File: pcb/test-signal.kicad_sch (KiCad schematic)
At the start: 36 parts, among them J5 731000105, U84 FSA553, U85 LM27761, U87 AD5683RARMZ, U94 MAX4489AUA+

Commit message: Update PCB component part numbers
Replace and fill missing MPN and OEPSPN properties.
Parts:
- C128: MPN (none) -> CC0402JRNPO9BN101; OEPSPN (none) -> OEPS010089
- C129, C131, C96: MPN (none) -> C0402C182J5RACTU; OEPSPN (none) -> OEPS010090
- C130, C132: MPN (none) -> DNP; OEPSPN (none) -> OEPS000000
- R267, R291: MPN RG1005P-104-B-T5 -> AC0402FR-07100KL; OEPSPN OEPS020175 -> OEPS020051
- R268: MPN RG1005P-104-B-T5 -> RMCF0402FT249K; OEPSPN OEPS020175 -> OEPS020209
- R269, R293, R294, R298, R299, R300: MPN (none) -> ERA-1AEB102C; OEPSPN (none) -> OEPS020189
- R292: MPN (none) -> RT0805BRE079KL; OEPSPN (none) -> OEPS020207
- R295, R296: MPN (none) -> RMCF0402FT10R0; OEPSPN (none) -> OEPS020205
- R297: MPN (none) -> PNM0402E5001BST1; OEPSPN (none) -> OEPS020206
- U84: MPN (none) -> FSA553UCX; OEPSPN (none) -> OEPS080198
- U85: MPN (none) -> LM27761DSGR; OEPSPN (none) -> OEPS080196
- U94: MPN (none) -> MAX4489AUA+; OEPSPN (none) -> OEPS080197
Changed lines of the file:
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@@
 			)
 		)
-		(property "MPN" ""
+		(property "MPN" "C0402C182J5RACTU"
 			(at 133.35 115.57 0)
 			(effects
@@
 			)
 		)
-		(property "OEPSPN" ""
+		(property "OEPSPN" "OEPS010090"
 			(at 133.35 115.57 0)
 			(effects
@@
 			)
 		)
+		(property "MPN" "MAX4489AUA+"
+			(at 161.29 36.83 0)
+			(effects
+				(font
+					(size 1.27 1.27)
+				)
+				(hide yes)
+			)
+		)
+		(property "OEPSPN" "OEPS080197"
+			(at 161.29 36.83 0)
+			(effects
+				(font
+					(size 1.27 1.27)
+				)
+				(hide yes)
+			)
+		)
 		(pin "3"
 		)
@@
 			)
 		)
-		(property "MPN" ""
+		(property "MPN" "DNP"
 			(at 157.48 73.66 0)
 			(effects
@@
 			)
 		)
-		(property "OEPSPN" ""
+		(property "OEPSPN" "OEPS000000"
 			(at 157.48 73.66 0)
 			(effects
@@
 			)
 		)
-		(property "MPN" ""
+		(property "MPN" "ERA-1AEB102C"
 			(at 195.58 104.14 0)
 			(effects
@@
 			)
 		)
-		(property "OEPSPN" ""
+		(property "OEPSPN" "OEPS020189"
 			(at 195.58 104.14 0)
 			(effects
@@
 			)
 		)
-		(property "MPN" ""
+		(property "MPN" "C0402C182J5RACTU"
 			(at 157.48 62.23 0)
 			(effects
@@
 			)
 		)
-		(property "OEPSPN" ""
+		(property "OEPSPN" "OEPS010090"
 			(at 157.48 62.23 0)
 			(effects
@@
 			)
 		)
+		(property "MPN" "FSA553UCX"
+			(at 80.01 34.29 0)
+			(effects
+				(font
+					(size 1.27 1.27)
+				)
+				(hide yes)
+			)
+		)
+		(property "OEPSPN" "OEPS080198"
+			(at 80.01 34.29 0)
+			(effects
+				(font
+					(size 1.27 1.27)
+				)
+				(hide yes)
+			)
+		)
 		(pin "C1"
 		)
@@
 			)
 		)
+		(property "MPN" "MAX4489AUA+"
+			(at 163.83 36.83 0)
+			(effects
+				(font
+					(size 1.27 1.27)
+				)
+				(hide yes)
+			)
+		)
+		(property "OEPSPN" "OEPS080197"
+			(at 163.83 36.83 0)
+			(effects
+				(font
+					(size 1.27 1.27)
+				)
+				(hide yes)
+			)
+		)
 		(pin "3"
 		)
@@
 			)
 		)
-		(property "MPN" ""
+		(property "MPN" "ERA-1AEB102C"
 			(at 157.48 82.55 0)
 			(effects
@@
 			)
 		)
-		(property "OEPSPN" ""
+		(property "OEPSPN" "OEPS020189"
 			(at 157.48 82.55 0)
 			(effects
@@
 			)
 		)
-		(property "MPN" "RG1005P-104-B-T5"
+		(property "MPN" "AC0402FR-07100KL"
 			(at 115.57 162.56 0)
 			(effects
@@
 			)
 		)
-		(property "OEPSPN" "OEPS020175"
+		(property "OEPSPN" "OEPS020051"
 			(at 115.57 162.56 0)
 			(effects
@@
 			)
 		)
-		(property "MPN" ""
+		(property "MPN" "RMCF0402FT10R0"
 			(at 127 36.83 0)
 			(effects
@@
 			)
 		)
-		(property "OEPSPN" ""
+		(property "OEPSPN" "OEPS020205"
 			(at 127 36.83 0)
 			(effects
@@
 			)
 		)
-		(property "MPN" "RG1005P-104-B-T5"
+		(property "MPN" "RMCF0402FT249K"
 			(at 97.79 175.26 0)
 			(effects
@@
 			)
 		)
-		(property "OEPSPN" "OEPS020175"
+		(property "OEPSPN" "OEPS020209"
 			(at 97.79 175.26 0)
 			(effects
@@
 			)
 		)
+		(property "MPN" "LM27761DSGR"
+			(at 69.85 165.1 0)
+			(effects
+				(font
+					(size 1.27 1.27)
+				)
+				(hide yes)
+			)
+		)
+		(property "OEPSPN" "OEPS080196"
+			(at 69.85 165.1 0)
+			(effects
+				(font
+					(size 1.27 1.27)
+				)
+				(hide yes)
+			)
+		)
 		(pin "1"
 		)
@@
 			)
 		)
-		(property "MPN" ""
+		(property "MPN" "ERA-1AEB102C"
 			(at 175.26 114.3 0)
 			(effects
@@
 			)
 		)
-		(property "OEPSPN" ""
+		(property "OEPSPN" "OEPS020189"
 			(at 175.26 114.3 0)
 			(effects
@@
 			)
 		)
-		(property "MPN" ""
+		(property "MPN" "RMCF0402FT10R0"
 			(at 113.03 106.68 0)
 			(effects
@@
 			)
 		)
-		(property "OEPSPN" ""
+		(property "OEPSPN" "OEPS020205"
 			(at 113.03 106.68 0)
 			(effects
@@
 			)
 		)
-		(property "MPN" ""
+		(property "MPN" "PNM0402E5001BST1"
 			(at 163.83 137.16 0)
 			(effects
@@
 			)
 		)
-		(property "OEPSPN" ""
+		(property "OEPSPN" "OEPS020206"
 			(at 163.83 137.16 0)
 			(effects
@@
 			)
 		)
-		(property "MPN" ""
+		(property "MPN" "ERA-1AEB102C"
 			(at 133.35 137.16 0)
 			(effects
@@
 			)
 		)
-		(property "OEPSPN" ""
+		(property "OEPSPN" "OEPS020189"
 			(at 133.35 137.16 0)
 			(effects
@@
 			)
 		)
-		(property "MPN" ""
+		(property "MPN" "CC0402JRNPO9BN101"
 			(at 191.77 45.72 0)
 			(effects
@@
 			)
 		)
-		(property "OEPSPN" ""
+		(property "OEPSPN" "OEPS010089"
 			(at 191.77 45.72 0)
 			(effects
@@
 			)
 		)
+		(property "MPN" "FSA553UCX"
+			(at 80.01 104.14 0)
+			(effects
+				(font
+					(size 1.27 1.27)
+				)
+				(hide yes)
+			)
+		)
+		(property "OEPSPN" "OEPS080198"
+			(at 80.01 104.14 0)
+			(effects
+				(font
+					(size 1.27 1.27)
+				)
+				(hide yes)
+			)
+		)
 		(pin "C1"
 		)
@@
 			)
 		)
-		(property "MPN" ""
+		(property "MPN" "C0402C182J5RACTU"
 			(at 162.56 115.57 0)
 			(effects
@@
 			)
 		)
-		(property "OEPSPN" ""
+		(property "OEPSPN" "OEPS010090"
 			(at 162.56 115.57 0)
 			(effects
@@
 			)
 		)
-		(property "MPN" ""
+		(property "MPN" "DNP"
 			(at 133.35 127 0)
 			(effects
@@
 			)
 		)
-		(property "OEPSPN" ""
+		(property "OEPSPN" "OEPS000000"
 			(at 133.35 127 0)
 			(effects
@@
 			)
 		)
-		(property "MPN" ""
+		(property "MPN" "ERA-1AEB102C"
 			(at 204.47 44.45 0)
 			(effects
@@
 			)
 		)
-		(property "OEPSPN" ""
+		(property "OEPSPN" "OEPS020189"
 			(at 204.47 44.45 0)
 			(effects
@@
 			)
 		)
-		(property "MPN" ""
+		(property "MPN" "RT0805BRE079KL"
 			(at 217.17 34.29 0)
 			(effects
@@
 			)
 		)
-		(property "OEPSPN" ""
+		(property "OEPSPN" "OEPS020207"
 			(at 217.17 34.29 0)
 			(effects
@@
 			)
 		)
-		(property "MPN" ""
+		(property "MPN" "ERA-1AEB102C"
 			(at 184.15 104.14 0)
 			(effects
@@
 			)
 		)
-		(property "OEPSPN" ""
+		(property "OEPSPN" "OEPS020189"
 			(at 184.15 104.14 0)
 			(effects
@@
 			)
 		)
-		(property "MPN" "RG1005P-104-B-T5"
+		(property "MPN" "AC0402FR-07100KL"
 			(at 105.41 162.56 0)
 			(effects
@@
 			)
 		)
-		(property "OEPSPN" "OEPS020175"
+		(property "OEPSPN" "OEPS020051"
 			(at 105.41 162.56 0)
 			(effects
@@
 			(at 135.89 106.68 0)
 			(effects
+				(font
+					(size 1.27 1.27)
+				)
+				(hide yes)
+			)
+		)
+		(property "MPN" "MAX4489AUA+"
+			(at 135.89 106.68 0)
+			(effects
+				(font
+					(size 1.27 1.27)
+				)
+				(hide yes)
+			)
+		)
+		(property "OEPSPN" "OEPS080197"
+			(at 135.89 106.68 0)
+			(effects

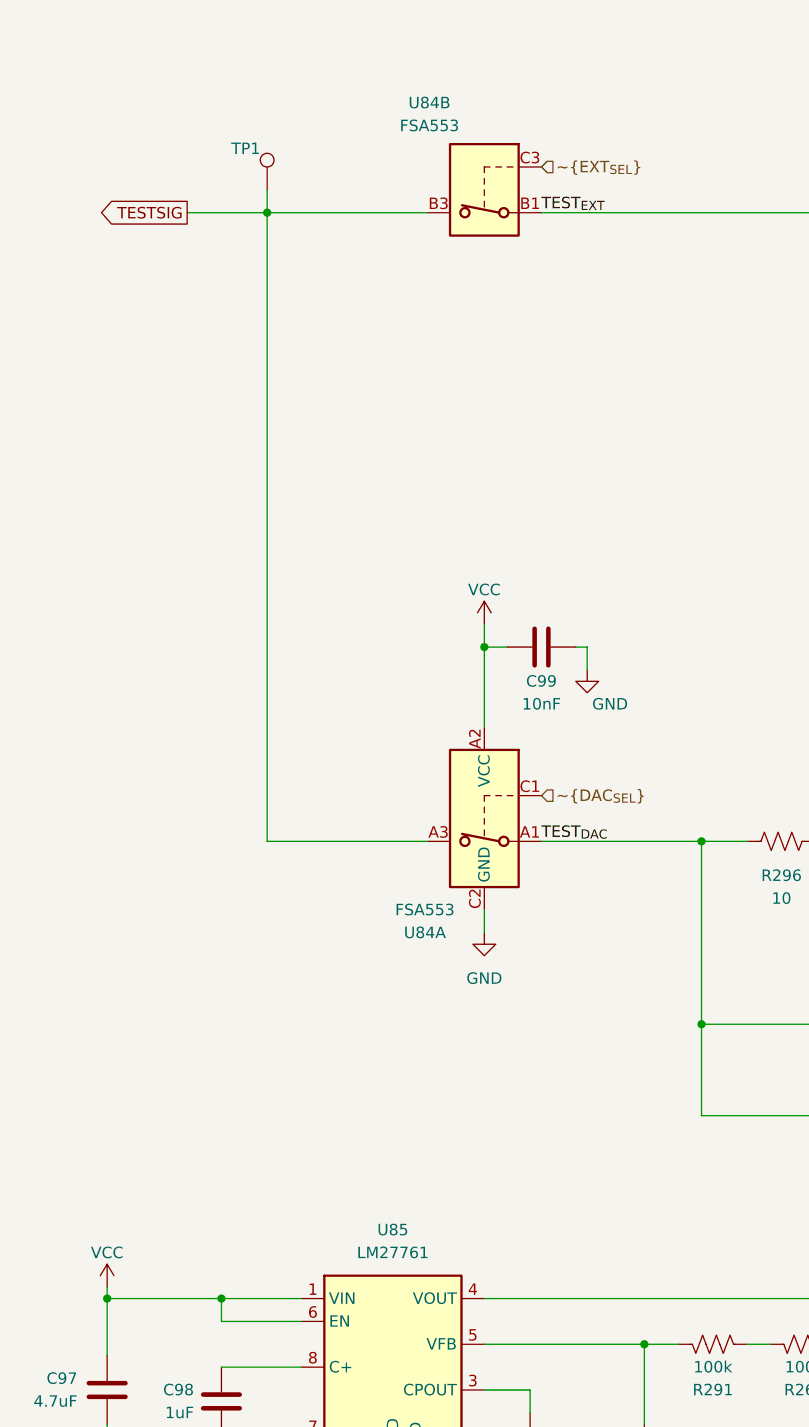
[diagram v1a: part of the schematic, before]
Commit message: Updated OEPS PN and regenerated BOM and PnP files
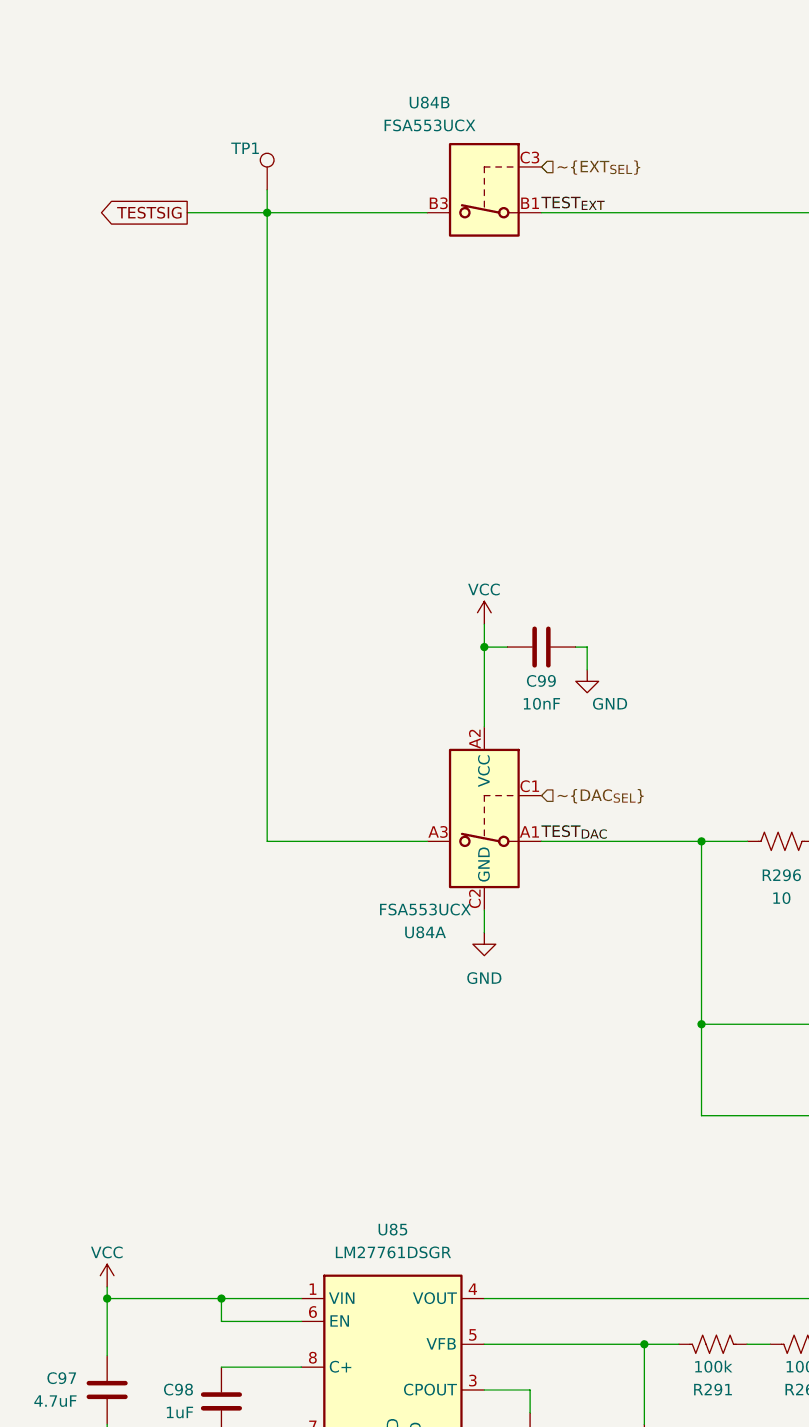
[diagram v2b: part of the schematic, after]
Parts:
- U84: value FSA553 -> FSA553UCX; LCSC (none) -> C605183
- U85: value LM27761 -> LM27761DSGR; LCSC (none) -> C129351
- U94: LCSC (none) -> C7451493
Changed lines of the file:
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@@
 			)
 		)
+		(property "LCSC" "C7451493"
+			(at 161.29 36.83 0)
+			(effects
+				(font
+					(size 1.27 1.27)
+				)
+				(hide yes)
+			)
+		)
 		(pin "3"
 		)
@@
 			)
 		)
-		(property "Value" "FSA553"
+		(property "Value" "FSA553UCX"
 			(at 73.914 27.178 0)
 			(effects
@@
 			)
 		)
+		(property "LCSC" "C605183 "
+			(at 80.01 34.29 0)
+			(effects
+				(font
+					(size 1.27 1.27)
+				)
+				(hide yes)
+			)
+		)
 		(pin "C1"
 		)
@@
 			)
 		)
+		(property "LCSC" "C7451493"
+			(at 163.83 36.83 0)
+			(effects
+				(font
+					(size 1.27 1.27)
+				)
+				(hide yes)
+			)
+		)
 		(pin "3"
 		)
@@
 			)
 		)
-		(property "Value" "LM27761"
+		(property "Value" "LM27761DSGR"
 			(at 69.85 152.4 0)
 			(effects
@@
 			)
 		)
+		(property "LCSC" "C129351 "
+			(at 69.85 165.1 0)
+			(effects
+				(font
+					(size 1.27 1.27)
+				)
+				(hide yes)
+			)
+		)
 		(pin "1"
 		)
@@
 			)
 		)
-		(property "Value" "FSA553"
+		(property "Value" "FSA553UCX"
 			(at 73.406 114.3 0)
 			(effects
@@
 			)
 		)
+		(property "LCSC" "C605183 "
+			(at 80.01 104.14 0)
+			(effects
+				(font
+					(size 1.27 1.27)
+				)
+				(hide yes)
+			)
+		)
 		(pin "C1"
 		)
@@
 			(at 135.89 106.68 0)
 			(effects
+				(font
+					(size 1.27 1.27)
+				)
+				(hide yes)
+			)
+		)
+		(property "LCSC" "C7451493"
+			(at 135.89 106.68 0)
+			(effects

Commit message: Rev. G production candidate
- Finished LCSC part numbers
- Generated final gerbers
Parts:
- C128: LCSC (none) -> C281751
- C129, C131, C96: LCSC (none) -> C107024
- R269, R293, R294, R298, R299, R300: LCSC (none) -> C852624
- R292: LCSC (none) -> C868262
- R295, R296: LCSC (none) -> C138066
- R297: LCSC (none) -> C5948099
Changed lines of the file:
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@@
 			)
 		)
-		(property "LCSC" ""
+		(property "LCSC" "C107024"
 			(at 133.35 115.57 90)
 			(effects
@@
 			)
 		)
-		(property "LCSC" ""
+		(property "LCSC" "C852624"
 			(at 195.58 104.14 90)
 			(effects
@@
 			)
 		)
-		(property "LCSC" ""
+		(property "LCSC" "C107024"
 			(at 157.48 62.23 90)
 			(effects
@@
 			)
 		)
-		(property "LCSC" ""
+		(property "LCSC" "C852624"
 			(at 157.48 82.55 90)
 			(effects
@@
 			)
 		)
-		(property "LCSC" ""
+		(property "LCSC" "C138066"
 			(at 127 36.83 90)
 			(effects
@@
 			)
 		)
-		(property "LCSC" ""
+		(property "LCSC" "C852624"
 			(at 175.26 114.3 90)
 			(effects
@@
 			)
 		)
-		(property "LCSC" ""
+		(property "LCSC" "C138066"
 			(at 113.03 106.68 90)
 			(effects
@@
 			)
 		)
-		(property "LCSC" ""
+		(property "LCSC" "C5948099"
 			(at 163.83 137.16 90)
 			(effects
@@
 			)
 		)
-		(property "LCSC" ""
+		(property "LCSC" "C852624"
 			(at 133.35 137.16 90)
 			(effects
@@
 			)
 		)
-		(property "LCSC" ""
+		(property "LCSC" "C281751"
 			(at 191.77 45.72 90)
 			(effects
@@
 			)
 		)
-		(property "LCSC" ""
+		(property "LCSC" "C107024"
 			(at 162.56 115.57 90)
 			(effects
@@
 			)
 		)
-		(property "LCSC" ""
+		(property "LCSC" "C852624"
 			(at 204.47 44.45 90)
 			(effects
@@
 			)
 		)
-		(property "LCSC" ""
+		(property "LCSC" "C868262"
 			(at 217.17 34.29 90)
 			(effects
@@
 			)
 		)
-		(property "LCSC" ""
+		(property "LCSC" "C852624"
 			(at 184.15 104.14 90)
 			(effects

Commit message: Minor BOM fix before production
Update the 1k 0402 resistor footprint/PN across BOM and schematics.
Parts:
- R269, R293, R294, R298, R299, R300: LCSC C852624 -> C2073397; MPN ERA-1AEB102C -> RG1005P-102-B-T5; OEPSPN OEPS020189 -> OEPS020219
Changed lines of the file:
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@@
 			)
 		)
-		(property "MPN" "ERA-1AEB102C"
+		(property "MPN" "RG1005P-102-B-T5"
 			(at 195.58 104.14 0)
 			(effects
@@
 			)
 		)
-		(property "OEPSPN" "OEPS020189"
+		(property "OEPSPN" "OEPS020219"
 			(at 195.58 104.14 0)
 			(effects
@@
 			)
 		)
-		(property "LCSC" "C852624"
+		(property "LCSC" "C2073397"
 			(at 195.58 104.14 90)
 			(effects
@@
 			)
 		)
-		(property "MPN" "ERA-1AEB102C"
+		(property "MPN" "RG1005P-102-B-T5"
 			(at 157.48 82.55 0)
 			(effects
@@
 			)
 		)
-		(property "OEPSPN" "OEPS020189"
+		(property "OEPSPN" "OEPS020219"
 			(at 157.48 82.55 0)
 			(effects
@@
 			)
 		)
-		(property "LCSC" "C852624"
+		(property "LCSC" "C2073397"
 			(at 157.48 82.55 90)
 			(effects
@@
 			)
 		)
-		(property "MPN" "ERA-1AEB102C"
+		(property "MPN" "RG1005P-102-B-T5"
 			(at 175.26 114.3 0)
 			(effects
@@
 			)
 		)
-		(property "OEPSPN" "OEPS020189"
+		(property "OEPSPN" "OEPS020219"
 			(at 175.26 114.3 0)
 			(effects
@@
 			)
 		)
-		(property "LCSC" "C852624"
+		(property "LCSC" "C2073397"
 			(at 175.26 114.3 90)
 			(effects
@@
 			)
 		)
-		(property "MPN" "ERA-1AEB102C"
+		(property "MPN" "RG1005P-102-B-T5"
 			(at 133.35 137.16 0)
 			(effects
@@
 			)
 		)
-		(property "OEPSPN" "OEPS020189"
+		(property "OEPSPN" "OEPS020219"
 			(at 133.35 137.16 0)
 			(effects
@@
 			)
 		)
-		(property "LCSC" "C852624"
+		(property "LCSC" "C2073397"
 			(at 133.35 137.16 90)
 			(effects
@@
 			)
 		)
-		(property "MPN" "ERA-1AEB102C"
+		(property "MPN" "RG1005P-102-B-T5"
 			(at 204.47 44.45 0)
 			(effects
@@
 			)
 		)
-		(property "OEPSPN" "OEPS020189"
+		(property "OEPSPN" "OEPS020219"
 			(at 204.47 44.45 0)
 			(effects
@@
 			)
 		)
-		(property "LCSC" "C852624"
+		(property "LCSC" "C2073397"
 			(at 204.47 44.45 90)
 			(effects
@@
 			)
 		)
-		(property "MPN" "ERA-1AEB102C"
+		(property "MPN" "RG1005P-102-B-T5"
 			(at 184.15 104.14 0)
 			(effects
@@
 			)
 		)
-		(property "OEPSPN" "OEPS020189"
+		(property "OEPSPN" "OEPS020219"
 			(at 184.15 104.14 0)
 			(effects
@@
 			)
 		)
-		(property "LCSC" "C852624"
+		(property "LCSC" "C2073397"
 			(at 184.15 104.14 90)
 			(effects

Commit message: Rev. G candidate
- Upgrade to KiCad 10
- Fix schematic comments
- Move html bom to pcb directory
- No changes in parts, no changes in part positions. Small internal
  routing changes for the switched cap inverter
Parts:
- C130, C132: value ~ -> (none)
